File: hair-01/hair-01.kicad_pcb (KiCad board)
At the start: 2 copper layers, 20 x 42.5 mm, 36 parts, among them J1 TYPE-C-31-M-12, Q1 BC847, Q2 BC847, Q3 2N7002, U1 ESP-12F, U2 AP2112K-3.3, U3 CP2102N-Axx-xQFN24, U4 TSMP58000

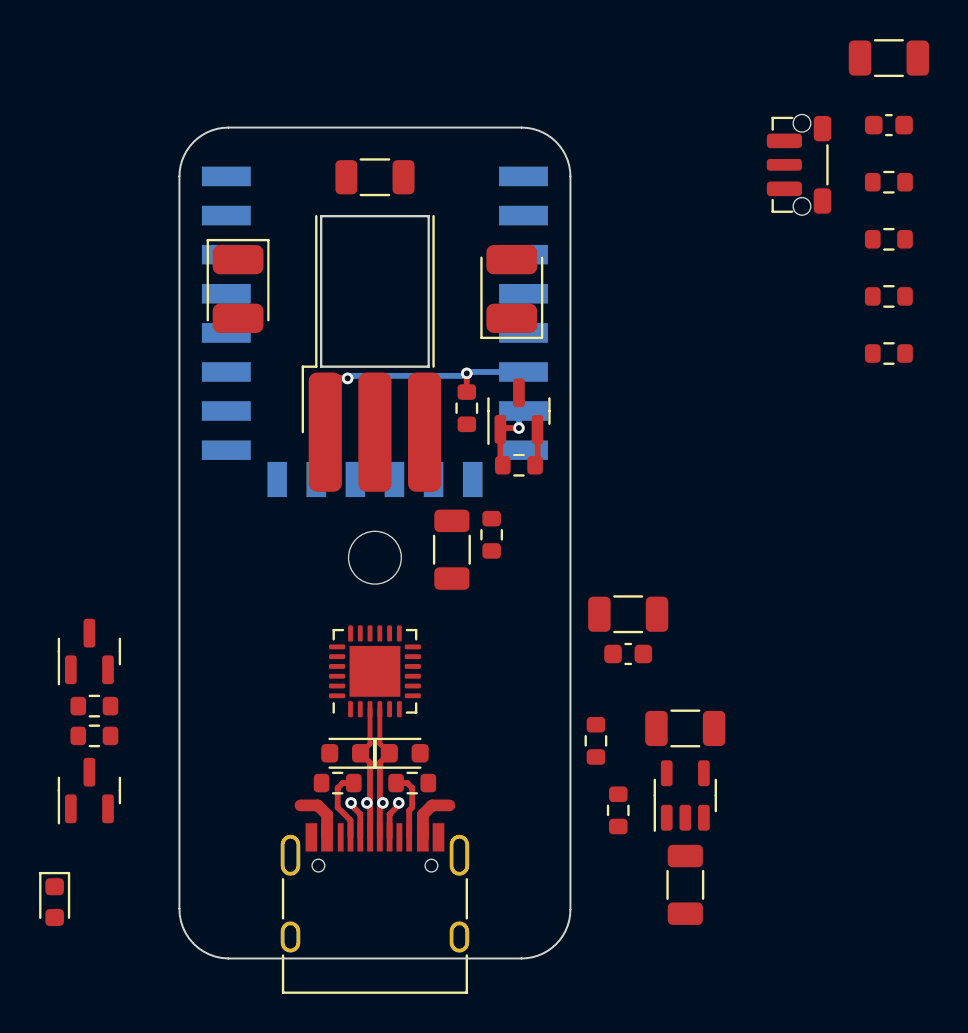
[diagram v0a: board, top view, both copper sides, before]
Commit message: hair-01: Replace reset button and more routing
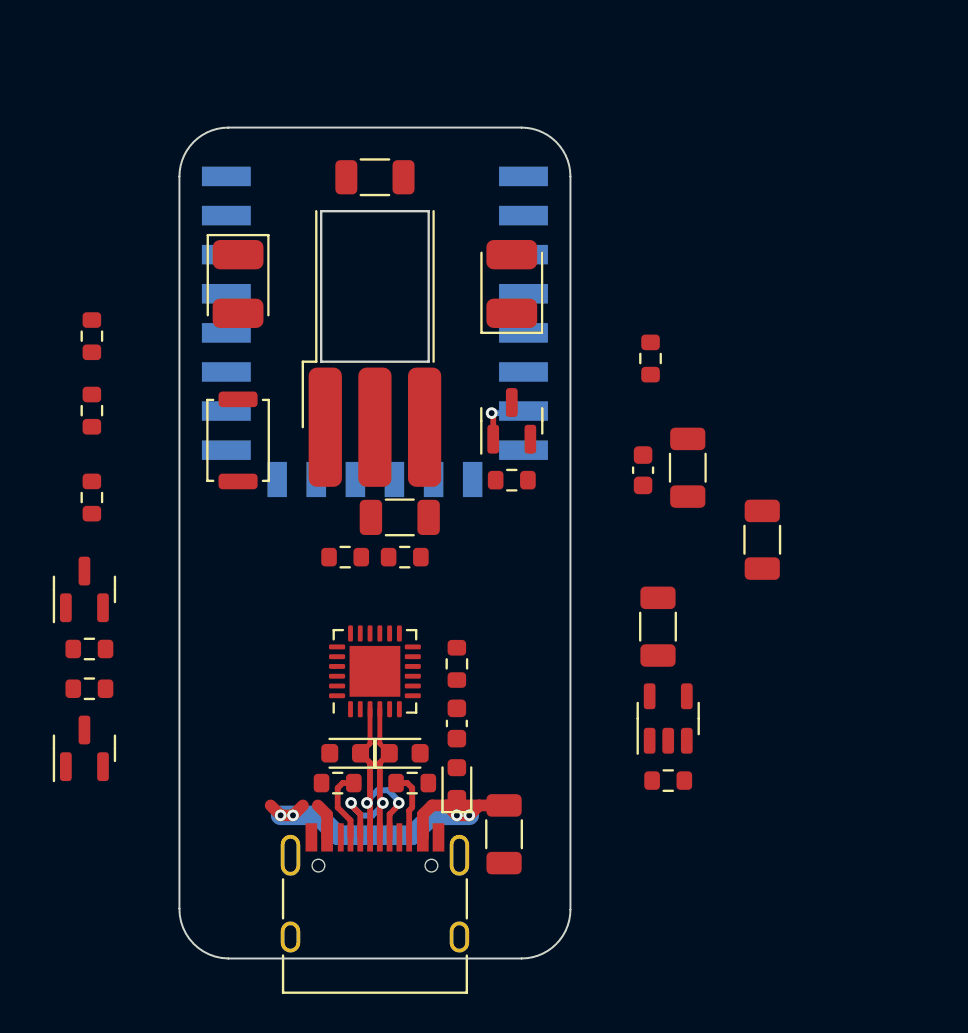
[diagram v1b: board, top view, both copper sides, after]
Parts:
- removed REF**: MountingHole_2.7mm_M2.5_DIN912_Keepout, hair-01:MountingHole_2.7mm_M2.5_DIN912_Keepout
- RST_SW1: footprint Button_Switch_SMD:SW_Push_1P1T-MP_NO_Horizontal_Alps_SKRTLAE010 -> Button_Switch_SMD:SW_Push_SPST_NO_Alps_SKRK
- moved R1 43.8 mm to (134.1, 95.1), turned to -90 degrees
- moved R4 40.9 mm to (134.1, 90.7), turned to -90 degrees
- moved R3 40.8 mm to (134.1, 86.9), turned to 90 degrees
- moved RST_SW1 32.1 mm to (141.6, 92.2)
- moved C1 23.3 mm to (164.6, 93.6), turned to -90 degrees
- moved C2 21.7 mm to (162.3, 93.7), turned to -90 degrees
- moved D3 21.5 mm to (152.8, 109.7), turned to 90 degrees
- moved R2 13.6 mm to (162.7, 88.0), turned to 90 degrees
- moved R12 9.84 mm to (147.1, 98.2), turned to 180 degrees
- moved C3 9.63 mm to (155.2, 112.3)
- moved C5 9.46 mm to (152.8, 106.7), turned to -90 degrees
- moved R10 8.13 mm to (152.8, 103.6), turned to 90 degrees
- moved C6 7.85 mm to (168.4, 97.3), turned to 90 degrees
- moved C4 5.39 mm to (163.1, 101.7), turned to 90 degrees
- moved R11 4.59 mm to (150.1, 98.2), turned to 180 degrees
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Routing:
- net VBUS: track 5.44 -> 22.0 mm, vias 0 -> 4
- net /IR_IN: track 13.5 -> 0.00 mm, vias 2 -> 0
- net /D-: track 9.04 -> 11.3 mm
- net /D+: track 9.04 -> 11.3 mm
- net GND: track 1.89 -> 0.00 mm
- net /IR_OUT: track 3.83 -> 3.04 mm

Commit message: hair-01: More routing
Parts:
- moved R3 13.1 mm to (141.9, 97.4), turned to 0 degrees
- moved R8 10.5 mm to (144.4, 103.8), turned to -90 degrees
- moved Q1 9.67 mm to (143.4, 107.3), turned to -90 degrees
- moved Q2 9.66 mm to (143.4, 100.2)
- moved R9 8.71 mm to (142.6, 103.8), turned to 90 degrees
- moved R1 7.78 mm to (141.9, 95.9), turned to 0 degrees
- moved R4 1.17 mm to (135.0, 91.4), turned to 0 degrees
- moved R7 0.92 mm to (163.8, 110.5), turned to 90 degrees
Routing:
- net VBUS: track 22.0 -> 53.4 mm
- net +3V3: track 0.00 -> 7.25 mm
- net /DTR: track 0.00 -> 6.66 mm
- net /RTS: track 0.00 -> 4.84 mm, vias 0 -> 2
- net /RESET: track 0.00 -> 3.78 mm
- net /RXD: track 0.00 -> 3.35 mm
- net Net-(R10-Pad2): track 0.00 -> 2.86 mm
- net /TXD: track 0.00 -> 2.49 mm
- net Net-(Q2-Pad1): track 0.00 -> 1.87 mm
- net Net-(Q1-Pad1): track 0.00 -> 1.82 mm

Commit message: hair-01: Routing done
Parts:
- moved R4 15.1 mm to (147.6, 99.8)
- moved C6 15.1 mm to (154.8, 103.9), turned to 0 degrees
- moved R2 12.5 mm to (153.2, 96.1), turned to 180 degrees
- moved C1 10.9 mm to (154.7, 98.2), turned to 180 degrees
- moved R7 9.56 mm to (155.6, 115.3), turned to 0 degrees
- moved C4 8.26 mm to (154.8, 101.5), turned to 0 degrees
- moved U2 8.08 mm to (155.6, 107.4)
- moved C2 6.56 mm to (156.2, 96.1), turned to 0 degrees
- moved R10 4.38 mm to (150.6, 99.8), turned to 180 degrees
- moved C7 1.02 mm to (148.8, 96.1)
- moved R11 0.51 mm to (150.6, 98.2)
- moved R12 0.51 mm to (147.6, 98.2)
- moved C3 0.43 mm to (155.6, 112.1)
- moved R13 0.25 mm to (155.6, 94.0)
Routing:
- net +3V3: track 7.25 -> 68.4 mm, vias 0 -> 3
- net /RESET: track 3.78 -> 34.1 mm, vias 0 -> 1
- net GND: track 0.00 -> 29.6 mm, vias 0 -> 19
- net /GPIO0: track 0.00 -> 26.7 mm, vias 0 -> 1
- net /TXD: track 2.49 -> 28.3 mm, vias 0 -> 1
- net /RXD: track 3.35 -> 26.9 mm, vias 0 -> 1
- net /IR_IN: track 0.00 -> 17.2 mm, vias 0 -> 1
- net Net-(R2-Pad2): track 0.00 -> 16.1 mm, vias 0 -> 1
- net Net-(R4-Pad1): track 0.00 -> 12.7 mm, vias 0 -> 1
- net Net-(D4-Pad1): track 0.00 -> 8.37 mm
- net Net-(D5-Pad2): track 0.00 -> 8.37 mm
- net Net-(C7-Pad1): track 0.00 -> 7.45 mm
- net VBUS: track 53.4 -> 60.9 mm
- net Net-(R7-Pad2): track 0.00 -> 7.26 mm
- net Net-(D5-Pad1): track 0.00 -> 4.55 mm
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- added copper zone on B.Cu, net GND

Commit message: hair-01: Add logo and name to silkscreen
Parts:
- added G***: LOGO, hair:Logo_6mm, B.Cu at (152.1, 101.7)
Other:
- board text added: "hair-01 icken.ch"
